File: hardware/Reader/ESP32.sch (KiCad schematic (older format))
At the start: 12 parts

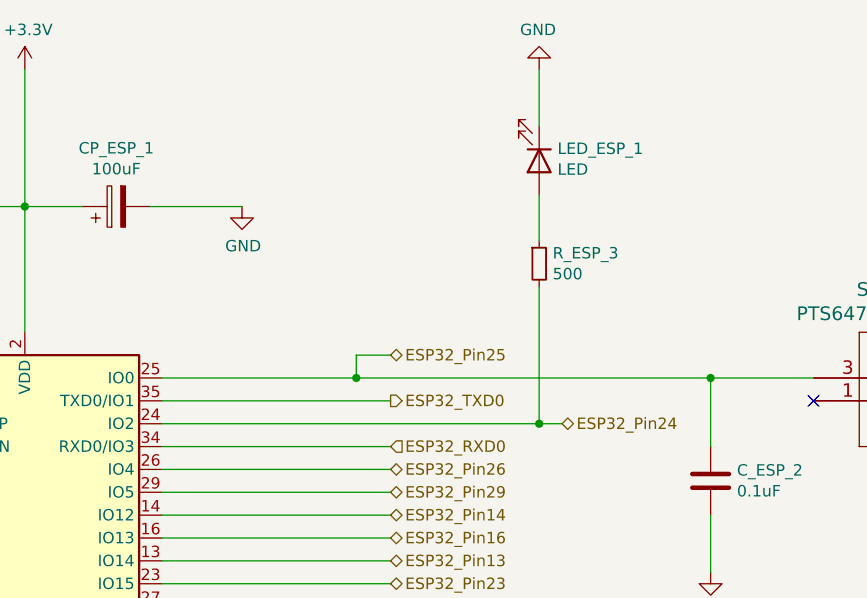
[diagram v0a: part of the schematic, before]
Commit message: Updated schematic and gerber to v0.0.05. Added ESP32. Removed MS CAN and SW CAN Transceivers. Added silkscreen text to header pins. Improved readability
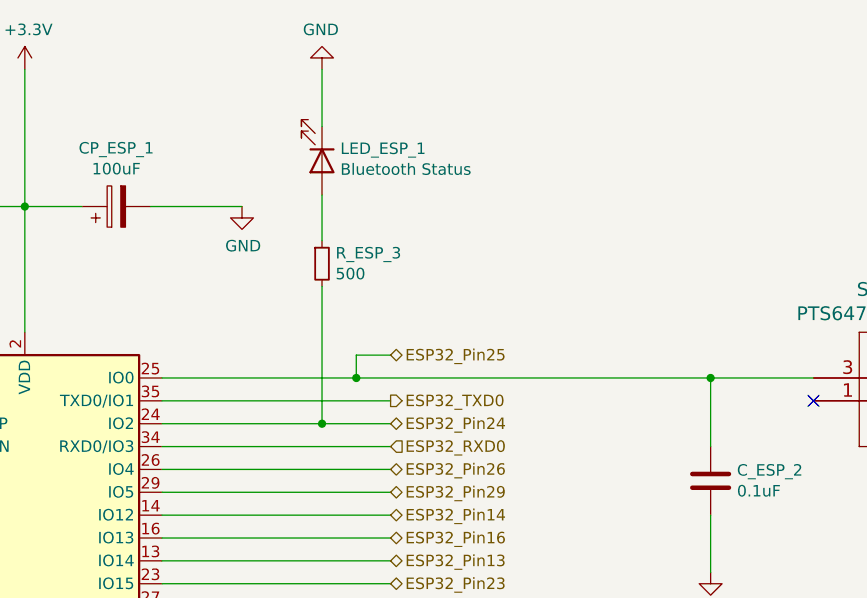
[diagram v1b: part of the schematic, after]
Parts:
- LED_ESP_1: value LED -> Bluetooth Status
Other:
- moved on the sheet: LED_ESP_1, R_ESP_3
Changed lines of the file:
@@
 $Descr A4 11693 8268
 encoding utf-8
-Sheet 3 17
+Sheet 10 17
 Title "CANnect Reader | ESP32"
-Date "2020-11-27"
+Date "2020-11-29"
 Rev "0.0.05"
 Comp "CANtech"
@@
 Wire Wire Line
 	8850 3300 8850 3050
-$Comp
-L Device:LED LED_ESP_1
-U 1 1 5FD157F7
-P 8100 1500
-F 0 "LED_ESP_1" V 8047 1580 50  0000 L CNN
-F 1 "LED" V 8138 1580 50  0000 L CNN
-F 2 "LED_SMD:LED_0603_1608Metric" H 8100 1500 50  0001 C CNN
-F 3 "https://www.we-online.de/katalog/datasheet/150060VS75000.pdf" H 8100 1500 50  0001 C CNN
-F 4 "Würth Elektronik" H 8100 1500 50  0001 C CNN "Manufacturer"
-F 5 "150060VS75000" H 8100 1500 50  0001 C CNN "Part Name"
-F 6 "DigiKey Canada" H 8100 1500 50  0001 C CNN "Vendor"
-F 7 "732-4980-1-ND" H 8100 1500 50  0001 C CNN "digikeypn"
-	1    8100 1500
-	0    1    1    0
-$EndComp
-$Comp
-L Device:R_Small R_ESP_3
-U 1 1 5FD162BA
-P 8100 1950
-F 0 "R_ESP_3" H 8159 1996 50  0000 L CNN
-F 1 "500" H 8159 1905 50  0000 L CNN
-F 2 "footprints:RESC1508X55N" H 8100 1950 50  0001 C CNN
-F 3 "https://www.vishay.com/docs/28916/mcxhp.pdf" H 8100 1950 50  0001 C CNN
-F 4 "Vishay" H 8100 1950 50  0001 C CNN "Manufacturer"
-F 5 "MCT0603PD4990DP500" H 8100 1950 50  0001 C CNN "Part Name"
-F 6 "DigiKey Canada" H 8100 1950 50  0001 C CNN "Vendor"
-F 7 "749-1523-1-ND" H 8100 1950 50  0001 C CNN "digikeypn"
-	1    8100 1950
-	1    0    0    -1
-$EndComp
-Wire Wire Line
-	6450 2650 8100 2650
-Wire Wire Line
-	8100 2650 8100 2050
-Wire Wire Line
-	8100 1650 8100 1850
-$Comp
-L power:GND #PWR0125
-U 1 1 5FD17BE0
-P 8100 1100
-F 0 "#PWR0125" H 8100 850 50  0001 C CNN
-F 1 "GND" H 8105 927 50  0000 C CNN
-F 2 "" H 8100 1100 50  0001 C CNN
-F 3 "" H 8100 1100 50  0001 C CNN
-	1    8100 1100
-	-1   0    0    1
-$EndComp
-Wire Wire Line
-	8100 1100 8100 1350
 Connection ~ 4100 2450
 Wire Wire Line
 	4100 2450 5250 2450
-Text HLabel 3950 2650 0    50   BiDi ~ 0
-ESP32_Pin4
-Text HLabel 3950 2750 0    50   BiDi ~ 0
-ESP32_Pin5
 Connection ~ 3050 2450
 Wire Wire Line
@@
 Wire Wire Line
 	3950 2750 5250 2750
-Text HLabel 3950 3650 0    50   BiDi ~ 0
-ESP32_Pin21
-Text HLabel 3950 3750 0    50   BiDi ~ 0
-ESP32_Pin22
-Text HLabel 3950 3850 0    50   BiDi ~ 0
-ESP32_Pin17
-Text HLabel 3950 3950 0    50   BiDi ~ 0
-ESP32_Pin18
-Text HLabel 3950 4050 0    50   BiDi ~ 0
-ESP32_Pin20
-Text HLabel 3950 4150 0    50   BiDi ~ 0
-ESP32_Pin19
 Wire Wire Line
 	5250 3650 3950 3650
@@
 Wire Wire Line
 	5850 5150 5850 5250
-Text HLabel 7450 2350 2    50   BiDi ~ 0
-ESP32_Pin25
 Text HLabel 7450 2550 2    50   Output ~ 0
 ESP32_TXD0
@@
 Wire Wire Line
 	7450 2550 6450 2550
-Text HLabel 7450 2750 2    50   Input ~ 0
-ESP32_RXD0
 Wire Wire Line
 	7450 2750 6450 2750
@@
 Wire Wire Line
 	6450 2850 7450 2850
+Wire Wire Line
+	7450 2950 6450 2950
+Wire Wire Line
+	7450 3050 6450 3050
+Wire Wire Line
+	7450 3150 6450 3150
+Wire Wire Line
+	7450 4750 6450 4750
+Wire Wire Line
+	6450 4650 7450 4650
+Wire Wire Line
+	7450 4550 6450 4550
+Wire Wire Line
+	6450 4450 7450 4450
+Wire Wire Line
+	7450 4350 6450 4350
+Wire Wire Line
+	6450 4250 7450 4250
+Wire Wire Line
+	7450 4150 6450 4150
+Wire Wire Line
+	6450 4050 7450 4050
+Wire Wire Line
+	7450 3950 6450 3950
+Wire Wire Line
+	6450 3850 7450 3850
+Wire Wire Line
+	7450 3450 6450 3450
+Wire Wire Line
+	6450 3550 7450 3550
+Wire Wire Line
+	7450 3650 6450 3650
+Wire Wire Line
+	6450 3750 7450 3750
+Wire Wire Line
+	7450 3250 6450 3250
+Wire Wire Line
+	7450 3350 6450 3350
+Wire Wire Line
+	8850 2750 8850 2450
+Connection ~ 8850 2450
+Wire Wire Line
+	8850 2450 9300 2450
+Text HLabel 7450 2750 2    50   Input ~ 0
+ESP32_RXD0
+Text HLabel 7450 4450 2    50   BiDi ~ 0
+ESP32_Pin8
+Text HLabel 7450 3950 2    50   BiDi ~ 0
+ESP32_Pin36
+Text HLabel 7450 3850 2    50   BiDi ~ 0
+ESP32_Pin33
+Text HLabel 7450 3750 2    50   BiDi ~ 0
+ESP32_Pin31
+Text HLabel 7450 3650 2    50   BiDi ~ 0
+ESP32_Pin30
+Text HLabel 7450 3550 2    50   BiDi ~ 0
+ESP32_Pin28
+Text HLabel 7450 3450 2    50   BiDi ~ 0
+ESP32_Pin27
+Text HLabel 7450 3350 2    50   BiDi ~ 0
+ESP32_Pin23
+Text HLabel 7450 3250 2    50   BiDi ~ 0
+ESP32_Pin13
+Text HLabel 7450 3150 2    50   BiDi ~ 0
+ESP32_Pin16
+Text HLabel 7450 3050 2    50   BiDi ~ 0
+ESP32_Pin14
 Text HLabel 7450 2950 2    50   BiDi ~ 0
 ESP32_Pin29
-Wire Wire Line
-	7450 2950 6450 2950
-Text HLabel 7450 3050 2    50   BiDi ~ 0
-ESP32_Pin14
-Wire Wire Line
-	7450 3050 6450 3050
-Text HLabel 7450 3150 2    50   BiDi ~ 0
-ESP32_Pin16
-Wire Wire Line
-	7450 3150 6450 3150
-Text HLabel 7450 3250 2    50   BiDi ~ 0
-ESP32_Pin13
-Text HLabel 7450 3350 2    50   BiDi ~ 0
-ESP32_Pin23
-Text HLabel 7450 3450 2    50   BiDi ~ 0
-ESP32_Pin27
-Text HLabel 7450 3550 2    50   BiDi ~ 0
-ESP32_Pin28
-Text HLabel 7450 3650 2    50   BiDi ~ 0
-ESP32_Pin30
-Text HLabel 7450 3750 2    50   BiDi ~ 0
-ESP32_Pin31
-Text HLabel 7450 3850 2    50   BiDi ~ 0
-ESP32_Pin33
-Text HLabel 7450 3950 2    50   BiDi ~ 0
-ESP32_Pin36
+$Comp
+L power:GND #PWR0125
+U 1 1 5FD17BE0
+P 7150 1100
+F 0 "#PWR0125" H 7150 850 50  0001 C CNN
+F 1 "GND" H 7155 927 50  0000 C CNN
+F 2 "" H 7150 1100 50  0001 C CNN
+F 3 "" H 7150 1100 50  0001 C CNN
+	1    7150 1100
+	-1   0    0    1
+$EndComp
+Wire Wire Line
+	6450 2650 7150 2650
+Wire Wire Line
+	7150 1100 7150 1350
+Wire Wire Line
+	7150 1650 7150 1850
+Wire Wire Line
+	7150 2650 7150 2050
+$Comp
+L Device:R_Small R_ESP_3
+U 1 1 5FD162BA
+P 7150 1950
+F 0 "R_ESP_3" H 7209 1996 50  0000 L CNN
+F 1 "500" H 7209 1905 50  0000 L CNN
+F 2 "footprints:RESC1508X55N" H 7150 1950 50  0001 C CNN
+F 3 "https://www.vishay.com/docs/28916/mcxhp.pdf" H 7150 1950 50  0001 C CNN
+F 4 "Vishay" H 7150 1950 50  0001 C CNN "Manufacturer"
+F 5 "MCT0603PD4990DP500" H 7150 1950 50  0001 C CNN "Part Name"
+F 6 "DigiKey Canada" H 7150 1950 50  0001 C CNN "Vendor"
+F 7 "749-1523-1-ND" H 7150 1950 50  0001 C CNN "digikeypn"
+	1    7150 1950
+	1    0    0    -1
+$EndComp
+$Comp
+L Device:LED LED_ESP_1
+U 1 1 5FD157F7
+P 7150 1500
+F 0 "LED_ESP_1" V 7097 1580 50  0000 L CNN
+F 1 "Bluetooth Status" V 7188 1580 50  0000 L CNN
+F 2 "LED_SMD:LED_0603_1608Metric" H 7150 1500 50  0001 C CNN
+F 3 "https://www.we-online.de/katalog/datasheet/150060VS75000.pdf" H 7150 1500 50  0001 C CNN
+F 4 "Würth Elektronik" H 7150 1500 50  0001 C CNN "Manufacturer"
+F 5 "150060VS75000" H 7150 1500 50  0001 C CNN "Part Name"
+F 6 "DigiKey Canada" H 7150 1500 50  0001 C CNN "Vendor"
+F 7 "732-4980-1-ND" H 7150 1500 50  0001 C CNN "digikeypn"
+	1    7150 1500
+	0    1    1    0
+$EndComp
+Text HLabel 3950 4150 0    50   BiDi ~ 0
+ESP32_Pin19
+Text HLabel 3950 4050 0    50   BiDi ~ 0
+ESP32_Pin20
+Text HLabel 3950 3950 0    50   BiDi ~ 0
+ESP32_Pin18
+Text HLabel 3950 3850 0    50   BiDi ~ 0
+ESP32_Pin17
+Text HLabel 3950 3750 0    50   BiDi ~ 0
+ESP32_Pin22
+Text HLabel 3950 3650 0    50   BiDi ~ 0
+ESP32_Pin21
+Text HLabel 3950 2750 0    50   BiDi ~ 0
+ESP32_Pin5
+Text HLabel 3950 2650 0    50   BiDi ~ 0
+ESP32_Pin4
 Text HLabel 7450 4050 2    50   BiDi ~ 0
 ESP32_Pin37
@@
 Text HLabel 7450 4350 2    50   BiDi ~ 0
 ESP32_Pin12
-Text HLabel 7450 4450 2    50   BiDi ~ 0
-ESP32_Pin8
 Text HLabel 7450 4550 2    50   BiDi ~ 0
 ESP32_Pin9
+Text HLabel 7450 4750 2    50   BiDi ~ 0
+ESP32_Pin7
 Text HLabel 7450 4650 2    50   BiDi ~ 0
 ESP32_Pin6
-Text HLabel 7450 4750 2    50   BiDi ~ 0
-ESP32_Pin7
-Wire Wire Line
-	7450 4750 6450 4750
-Wire Wire Line
-	6450 4650 7450 4650
-Wire Wire Line
-	7450 4550 6450 4550
-Wire Wire Line
-	6450 4450 7450 4450
-Wire Wire Line
-	7450 4350 6450 4350
-Wire Wire Line
-	6450 4250 7450 4250
-Wire Wire Line
-	7450 4150 6450 4150
-Wire Wire Line
-	6450 4050 7450 4050
-Wire Wire Line
-	7450 3950 6450 3950
-Wire Wire Line
-	6450 3850 7450 3850
-Wire Wire Line
-	7450 3450 6450 3450
-Wire Wire Line
-	6450 3550 7450 3550
-Wire Wire Line
-	7450 3650 6450 3650
-Wire Wire Line
-	6450 3750 7450 3750
-Wire Wire Line
-	7450 3250 6450 3250
-Wire Wire Line
-	7450 3350 6450 3350
-Text HLabel 8200 2650 2    50   BiDi ~ 0
+Text HLabel 7450 2650 2    50   BiDi ~ 0
 ESP32_Pin24
-Wire Wire Line
-	8200 2650 8100 2650
-Connection ~ 8100 2650
-Wire Wire Line
-	8850 2750 8850 2450
-Connection ~ 8850 2450
-Wire Wire Line
-	8850 2450 9300 2450
+Text HLabel 7450 2350 2    50   BiDi ~ 0
+ESP32_Pin25
+Connection ~ 7150 2650
+Wire Wire Line
+	7150 2650 7450 2650
 $EndSCHEMATC

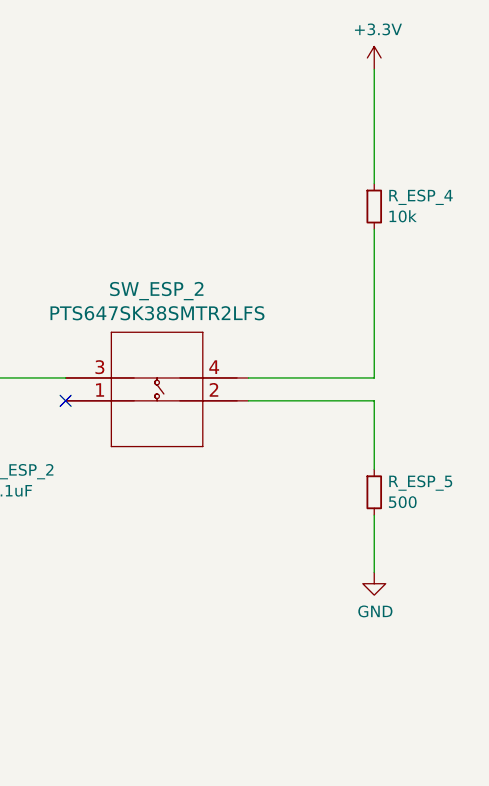
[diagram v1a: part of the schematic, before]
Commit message: Converted PCB design into a 2-layer PCB for v0.0.5b. Adjusted schematic to use header pins for connector
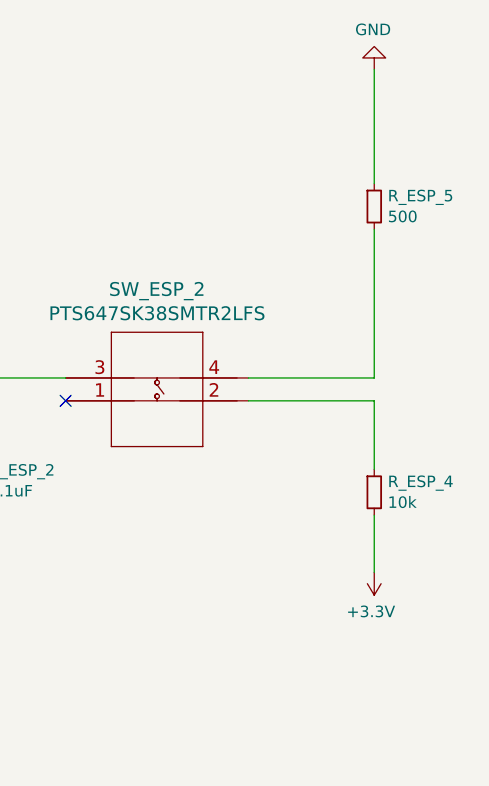
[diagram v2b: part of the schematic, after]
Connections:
- net +3V3: now also R_ESP_4.2; no longer R_ESP_4.1
- net GND: now also R_ESP_5.1; no longer R_ESP_5.2
- net at SW_ESP_2.2: now also R_ESP_4.1; no longer R_ESP_5.1
- net at SW_ESP_2.4: now also R_ESP_5.2; no longer R_ESP_4.2
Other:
- moved on the sheet: R_ESP_4, R_ESP_5
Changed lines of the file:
@@
 L Device:R_Small R_ESP_4
 U 1 1 5FD0B524
-P 10650 1700
-F 0 "R_ESP_4" H 10709 1746 50  0000 L CNN
-F 1 "10k" H 10709 1655 50  0000 L CNN
-F 2 "footprints:RESC1608X55N" H 10650 1700 50  0001 C CNN
-F 3 "https://www.yageo.com/upload/media/product/productsearch/datasheet/rchip/PYu-RT_1-to-0.01_RoHS_L_12.pdf" H 10650 1700 50  0001 C CNN
-F 4 "Yageo" H 10650 1700 50  0001 C CNN "Manufacturer"
-F 5 "RT0603FRE0710KL" H 10650 1700 50  0001 C CNN "Part Name"
-F 6 "DigiKey Canada" H 10650 1700 50  0001 C CNN "Vendor"
-F 7 "YAG2321CT-ND" H 10650 1700 50  0001 C CNN "digikeypn"
-	1    10650 1700
+P 10650 2950
+F 0 "R_ESP_4" H 10709 2996 50  0000 L CNN
+F 1 "10k" H 10709 2905 50  0000 L CNN
+F 2 "footprints:RESC1608X55N" H 10650 2950 50  0001 C CNN
+F 3 "https://www.yageo.com/upload/media/product/productsearch/datasheet/rchip/PYu-RT_1-to-0.01_RoHS_L_12.pdf" H 10650 2950 50  0001 C CNN
+F 4 "Yageo" H 10650 2950 50  0001 C CNN "Manufacturer"
+F 5 "RT0603FRE0710KL" H 10650 2950 50  0001 C CNN "Part Name"
+F 6 "DigiKey Canada" H 10650 2950 50  0001 C CNN "Vendor"
+F 7 "YAG2321CT-ND" H 10650 2950 50  0001 C CNN "digikeypn"
+	1    10650 2950
 	1    0    0    -1
 $EndComp
@@
 L Device:R_Small R_ESP_5
 U 1 1 5FD0B52A
-P 10650 2950
-F 0 "R_ESP_5" H 10709 2996 50  0000 L CNN
-F 1 "500" H 10709 2905 50  0000 L CNN
-F 2 "footprints:RESC1508X55N" H 10650 2950 50  0001 C CNN
-F 3 "https://www.vishay.com/docs/28916/mcxhp.pdf" H 10650 2950 50  0001 C CNN
-F 4 "Vishay" H 10650 2950 50  0001 C CNN "Manufacturer"
-F 5 "MCT0603PD4990DP500" H 10650 2950 50  0001 C CNN "Part Name"
-F 6 "DigiKey Canada" H 10650 2950 50  0001 C CNN "Vendor"
-F 7 "749-1523-1-ND" H 10650 2950 50  0001 C CNN "digikeypn"
-	1    10650 2950
+P 10650 1700
+F 0 "R_ESP_5" H 10709 1746 50  0000 L CNN
+F 1 "500" H 10709 1655 50  0000 L CNN
+F 2 "footprints:RESC1508X55N" H 10650 1700 50  0001 C CNN
+F 3 "https://www.vishay.com/docs/28916/mcxhp.pdf" H 10650 1700 50  0001 C CNN
+F 4 "Vishay" H 10650 1700 50  0001 C CNN "Manufacturer"
+F 5 "MCT0603PD4990DP500" H 10650 1700 50  0001 C CNN "Part Name"
+F 6 "DigiKey Canada" H 10650 1700 50  0001 C CNN "Vendor"
+F 7 "749-1523-1-ND" H 10650 1700 50  0001 C CNN "digikeypn"
+	1    10650 1700
 	1    0    0    -1
 $EndComp
@@
 L power:+3.3V #PWR0121
 U 1 1 5FD0B534
-P 10650 1100
-F 0 "#PWR0121" H 10650 950 50  0001 C CNN
-F 1 "+3.3V" H 10665 1273 50  0000 C CNN
-F 2 "" H 10650 1100 50  0001 C CNN
-F 3 "" H 10650 1100 50  0001 C CNN
-	1    10650 1100
-	1    0    0    -1
+P 10650 3300
+F 0 "#PWR0121" H 10650 3150 50  0001 C CNN
+F 1 "+3.3V" H 10665 3473 50  0000 C CNN
+F 2 "" H 10650 3300 50  0001 C CNN
+F 3 "" H 10650 3300 50  0001 C CNN
+	1    10650 3300
+	-1   0    0    1
 $EndComp
 Wire Wire Line
@@
 L power:GND #PWR0122
 U 1 1 5FD0B53B
-P 10650 3300
-F 0 "#PWR0122" H 10650 3050 50  0001 C CNN
-F 1 "GND" H 10655 3127 50  0000 C CNN
-F 2 "" H 10650 3300 50  0001 C CNN
-F 3 "" H 10650 3300 50  0001 C CNN
-	1    10650 3300
-	1    0    0    -1
+P 10650 1100
+F 0 "#PWR0122" H 10650 850 50  0001 C CNN
+F 1 "GND" H 10655 927 50  0000 C CNN
+F 2 "" H 10650 1100 50  0001 C CNN
+F 3 "" H 10650 1100 50  0001 C CNN
+	1    10650 1100
+	-1   0    0    1
 $EndComp
 Wire Wire Line
